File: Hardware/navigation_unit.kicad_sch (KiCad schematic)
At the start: 36 parts, among them SW1 SW_SPDT, SW2 SW_Push_Dual, U4 STM32F405RGTx, Y1 25MHz

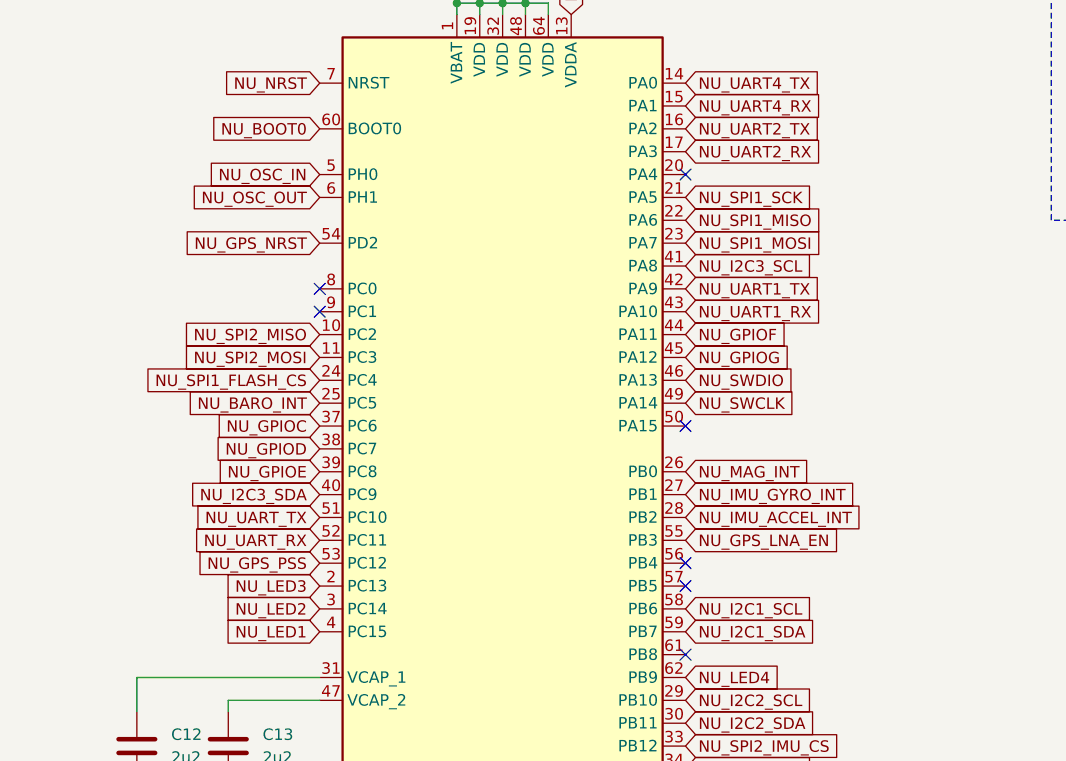
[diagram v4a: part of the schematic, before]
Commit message: version 0.1.1, added dfu usb to firmware upload, changed pwm channels
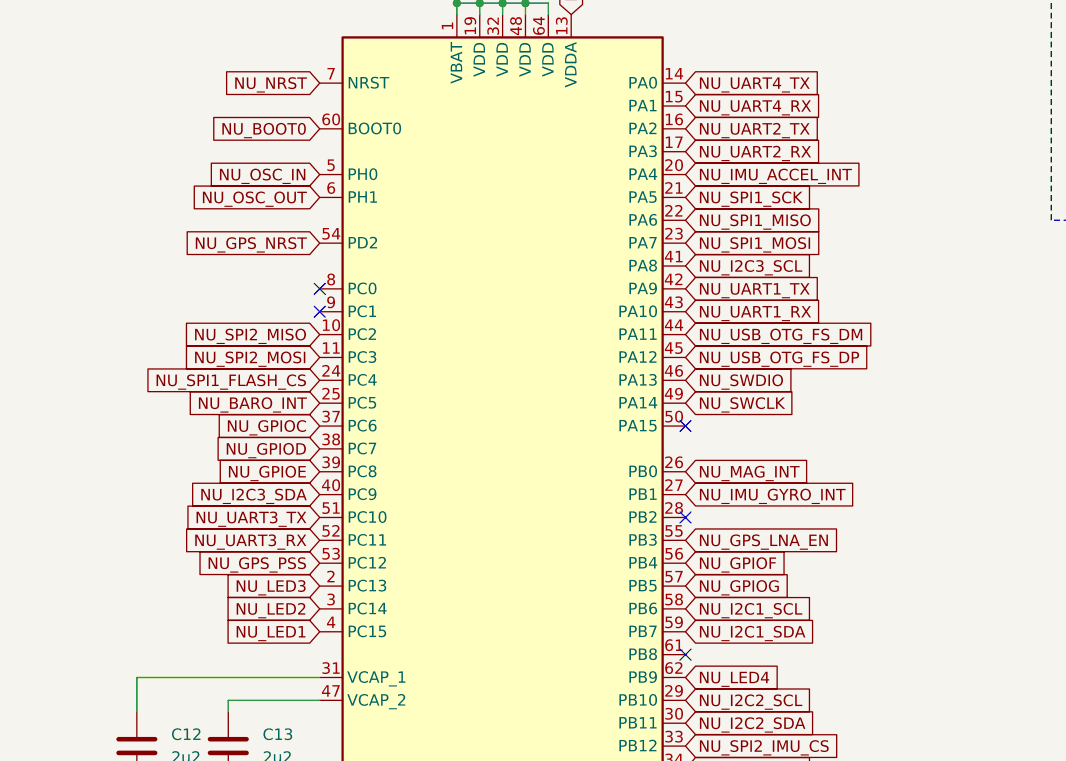
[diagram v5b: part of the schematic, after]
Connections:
- net NU_GPIOF: now also U4.56 (PB4); no longer U4.44 (PA11)
- net NU_GPIOG: now also U4.57 (PB5); no longer U4.45 (PA12)
- net NU_IMU_ACCEL_INT: now also U4.20 (PA4); no longer U4.28 (PB2)
- net NU_UART_RX renamed NU_UART3_RX
- net NU_UART_TX renamed NU_UART3_TX
- new net NU_USB_OTG_FS_DM: U4.44 (PA11)
- new net NU_USB_OTG_FS_DP: U4.45 (PA12)
- no-connect marks 7 -> 5

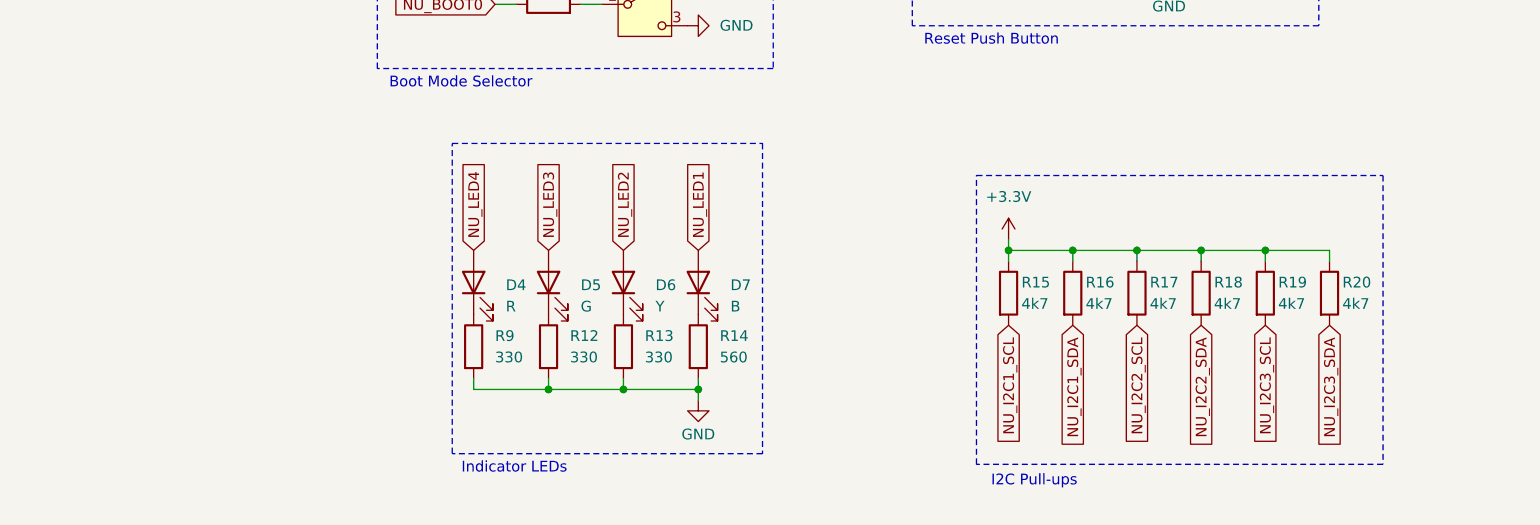
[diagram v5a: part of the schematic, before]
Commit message: added nu i2c test point, some documentation hehe
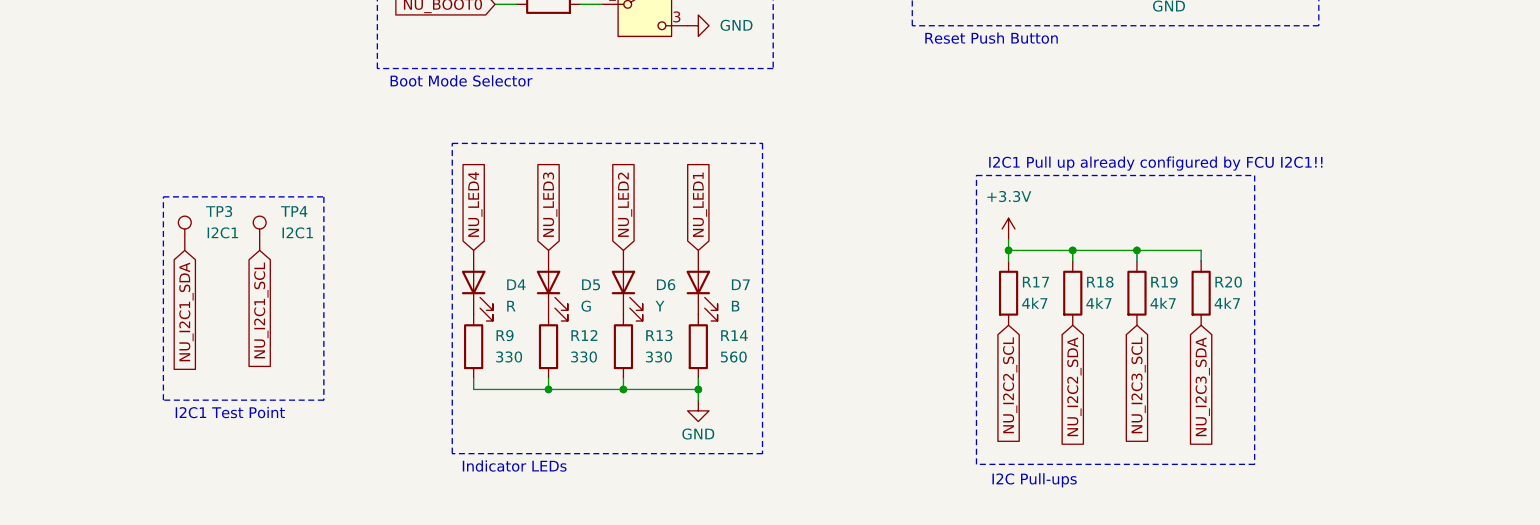
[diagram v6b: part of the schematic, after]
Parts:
- removed R15, R16: 4k7, symbol Device:R
- added TP3, TP4: I2C1, symbol Connector:TestPoint
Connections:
- net NU_I2C1_SCL: now also TP4.1
- net NU_I2C1_SDA: now also TP3.1
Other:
- note added: "I2C1 Pull up already configured by FCU I2C1!!"
- note added: "I2C1 Test Point"
- moved on the sheet: R17, R18, R19, R20

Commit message: pin refatoration, freertos code
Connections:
- net NU_BARO_INT: now also U4.4 (PC15); no longer U4.25 (PC5)
- net NU_GPS_LNA_EN: now also U4.24 (PC4); no longer U4.55 (PB3)
- net NU_GPS_NRST: now also U4.25 (PC5); no longer U4.54 (PD2)
- net NU_GPS_PSS: now also U4.26 (PB0); no longer U4.53 (PC12)
- net NU_I2C1_SCL: now also U4.61 (PB8); no longer U4.58 (PB6)
- net NU_I2C1_SDA: now also U4.62 (PB9); no longer U4.59 (PB7)
- net NU_IMU_ACCEL_INT: now also U4.2 (PC13); no longer U4.20 (PA4)
- net NU_IMU_GYRO_INT: now also U4.3 (PC14); no longer U4.27 (PB1)
- net NU_LED1: no longer U4.4 (PC15)
- net NU_LED2: no longer U4.3 (PC14)
- net NU_LED3: no longer U4.2 (PC13)
- net NU_LED4: no longer U4.62 (PB9)
- net NU_MAG_INT: now also U4.8 (PC0); no longer U4.26 (PB0)
- net NU_SPI1_FLASH_CS: now also U4.20 (PA4); no longer U4.24 (PC4)
- net NU_UART1_RX: now also U4.59 (PB7); no longer U4.43 (PA10)
- net NU_UART1_TX: now also U4.58 (PB6); no longer U4.42 (PA9)
- net NU_GPIO_F: now reaches U4.50 (PA15)
- net NU_GPIOA renamed NU_LED_4
- net NU_GPIOB renamed NU_LED_3
- net NU_GPIOC renamed NU_LED_2
- net NU_GPIOD renamed NU_LED_1
- net NU_GPIOE: no longer names the net of U4.39 (PC8)
- net NU_GPIOF renamed NU_GPIO_B
- net NU_GPIOG renamed NU_GPIO_A
- net NU_SPI2_IMU_CS renamed NU_SPI2_CS_IMU
- new net NU_GPIO_C: U4.55 (PB3)
- new net NU_GPIO_D: U4.54 (PD2)
- new net NU_GPIO_E: U4.53 (PC12)
- new net NU_USB_OTG_ID: U4.43 (PA10)
- new net NU_USB_OTG_VBUS: U4.42 (PA9)
- no-connect marks 5 -> 4

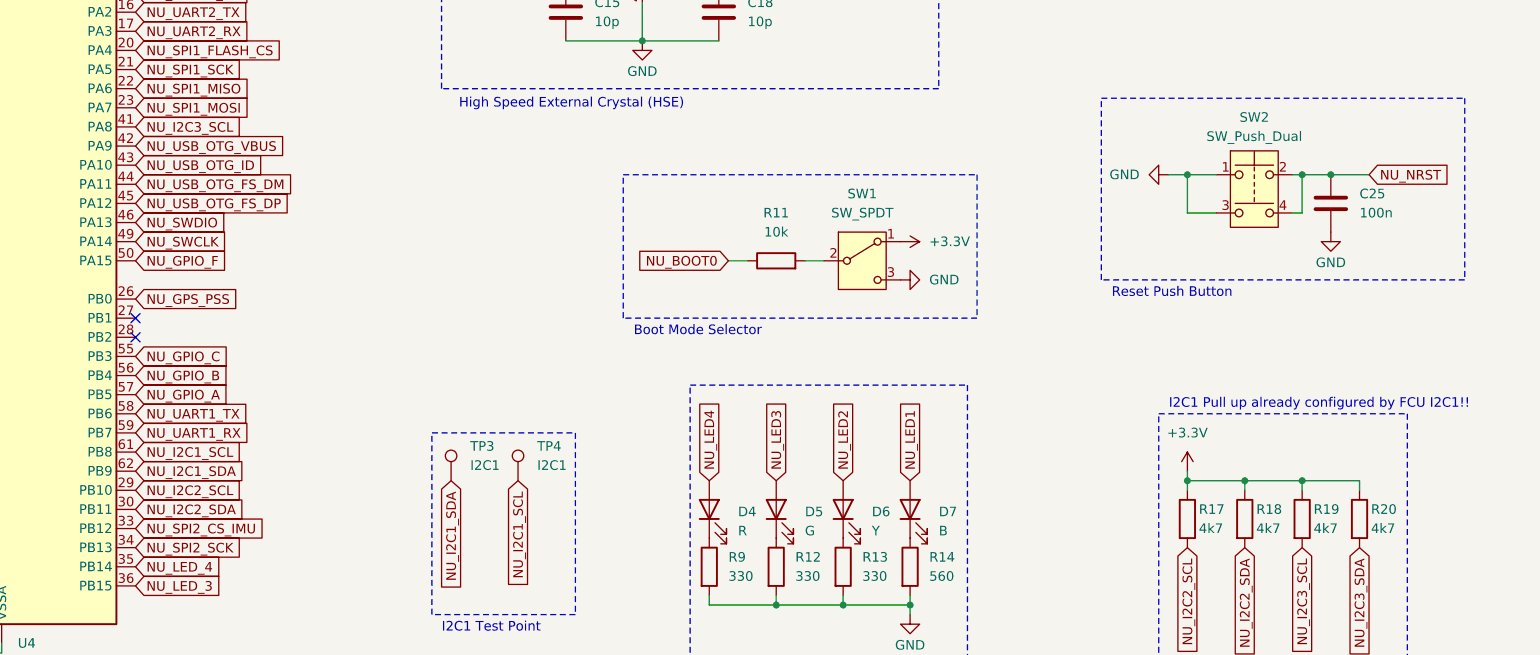
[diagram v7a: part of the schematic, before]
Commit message: add some footprints, and pcb configs
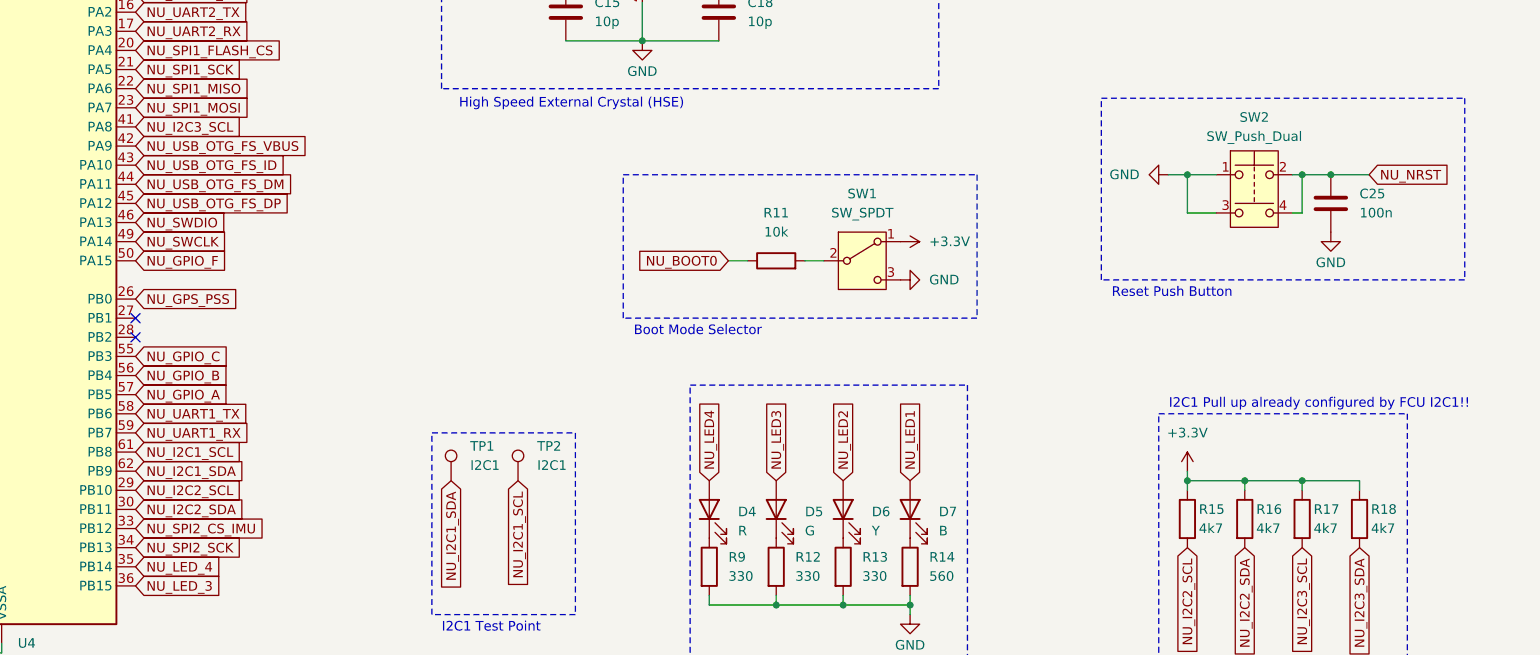
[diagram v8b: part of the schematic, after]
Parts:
- C12, C13, C25: footprint (none) -> Capacitor_SMD:C_0603_1608Metric
- C14, C26: footprint (none) -> Capacitor_Tantalum_SMD:CP_EIA-1608-08_AVX-J
- C15, C16, C17, C18, C19, C20, C21, C22, C23, C24: footprint (none) -> Capacitor_SMD:C_0402_1005Metric
- D4, D5, D6, D7: footprint (none) -> LED_SMD:LED_0805_2012Metric
- FB1: footprint (none) -> Inductor_SMD:L_0805_2012Metric
- R10, R11, R12, R13, R14, R9: footprint (none) -> Resistor_SMD:R_0603_1608Metric_Pad0.98x0.95mm_HandSolder
- R15: renamed from R17; footprint (none) -> Resistor_SMD:R_0603_1608Metric_Pad0.98x0.95mm_HandSolder
- R16: renamed from R18; footprint (none) -> Resistor_SMD:R_0603_1608Metric_Pad0.98x0.95mm_HandSolder
- R17: renamed from R19; footprint (none) -> Resistor_SMD:R_0603_1608Metric_Pad0.98x0.95mm_HandSolder
- R18: renamed from R20; footprint (none) -> Resistor_SMD:R_0603_1608Metric_Pad0.98x0.95mm_HandSolder
- TP1: renamed from TP3; footprint (none) -> TestPoint:TestPoint_Pad_D2.5mm
- TP2: renamed from TP4; footprint (none) -> TestPoint:TestPoint_Pad_D2.5mm
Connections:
- net NU_USB_OTG_ID renamed NU_USB_OTG_FS_ID
- net NU_USB_OTG_VBUS renamed NU_USB_OTG_FS_VBUS
